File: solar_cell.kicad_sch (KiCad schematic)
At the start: 17 parts, among them U5 LM324, U6 4046

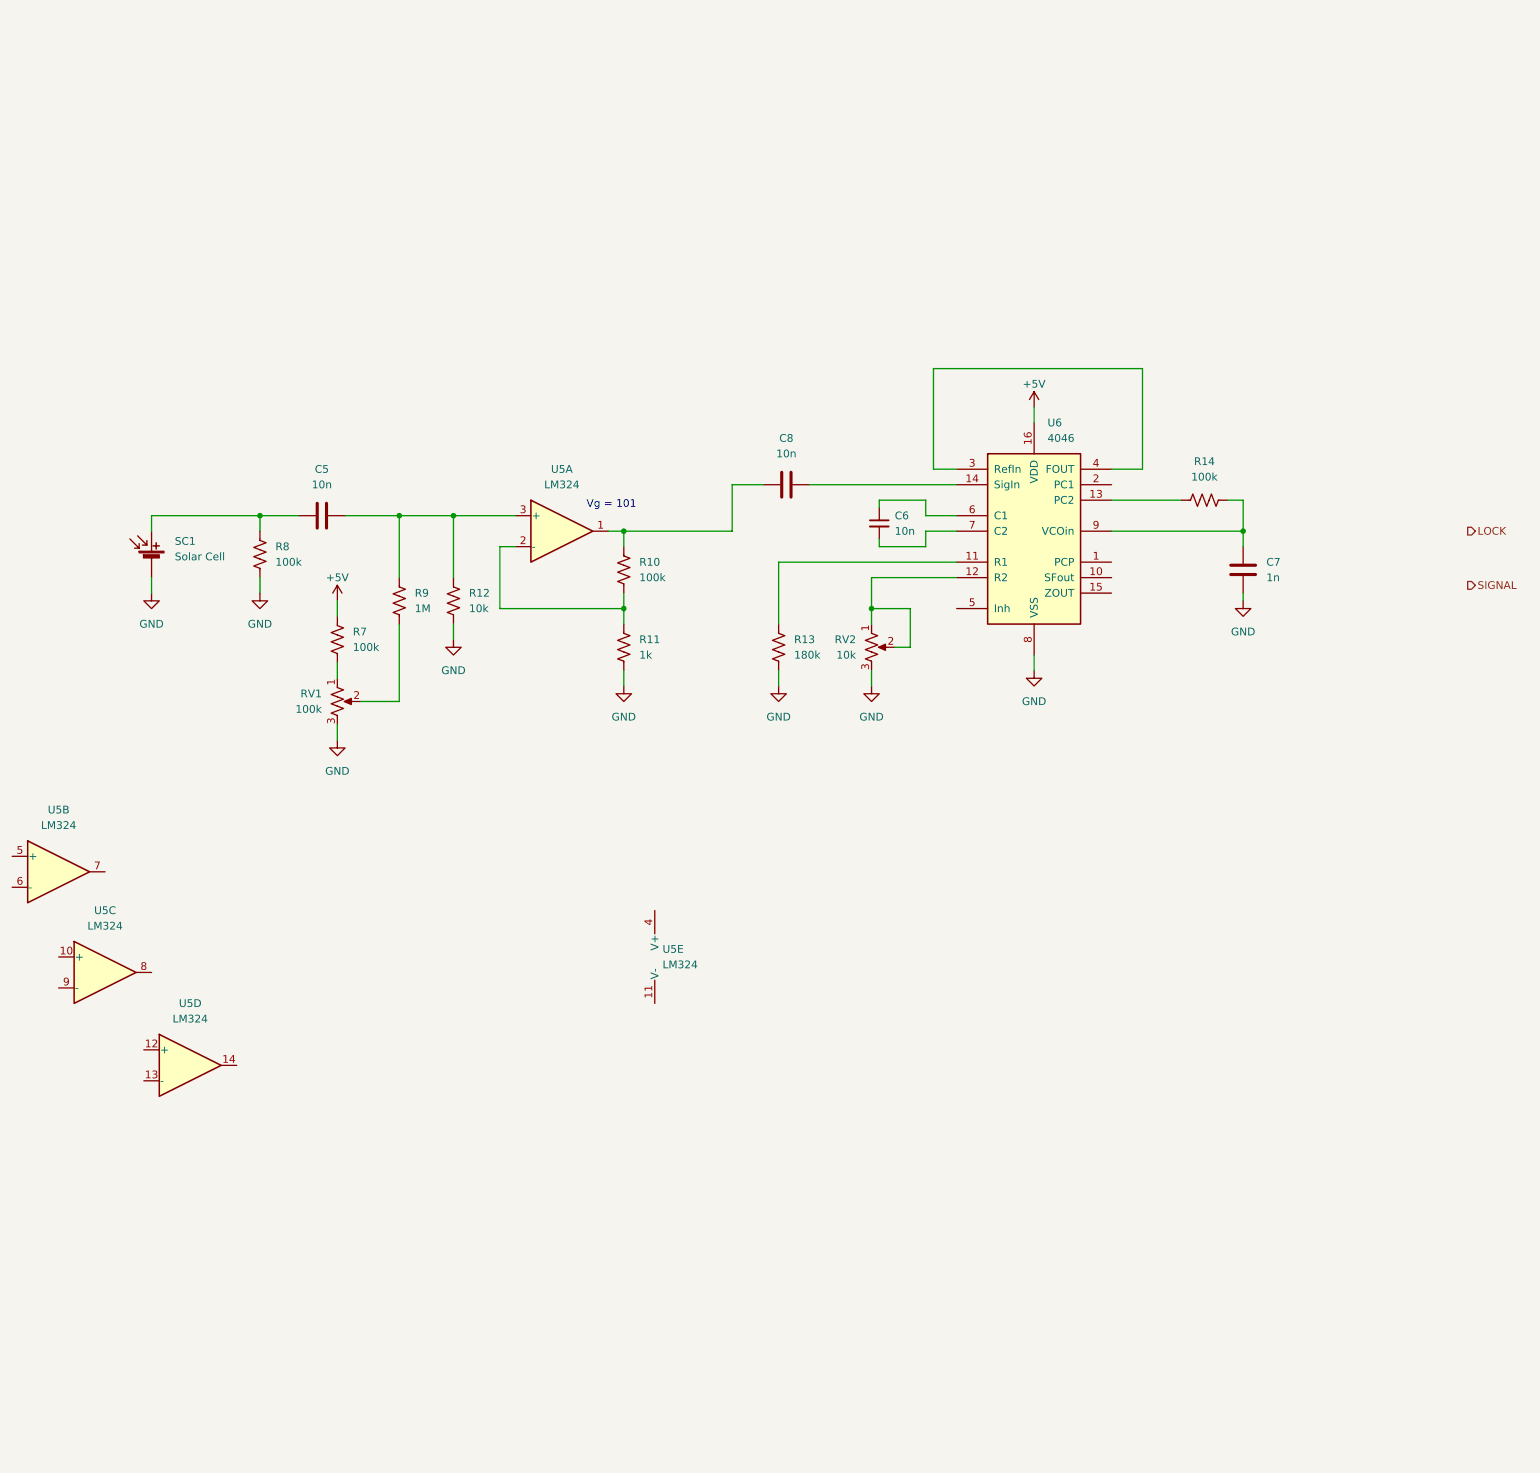
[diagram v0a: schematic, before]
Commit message: BUtton logic and solar detection
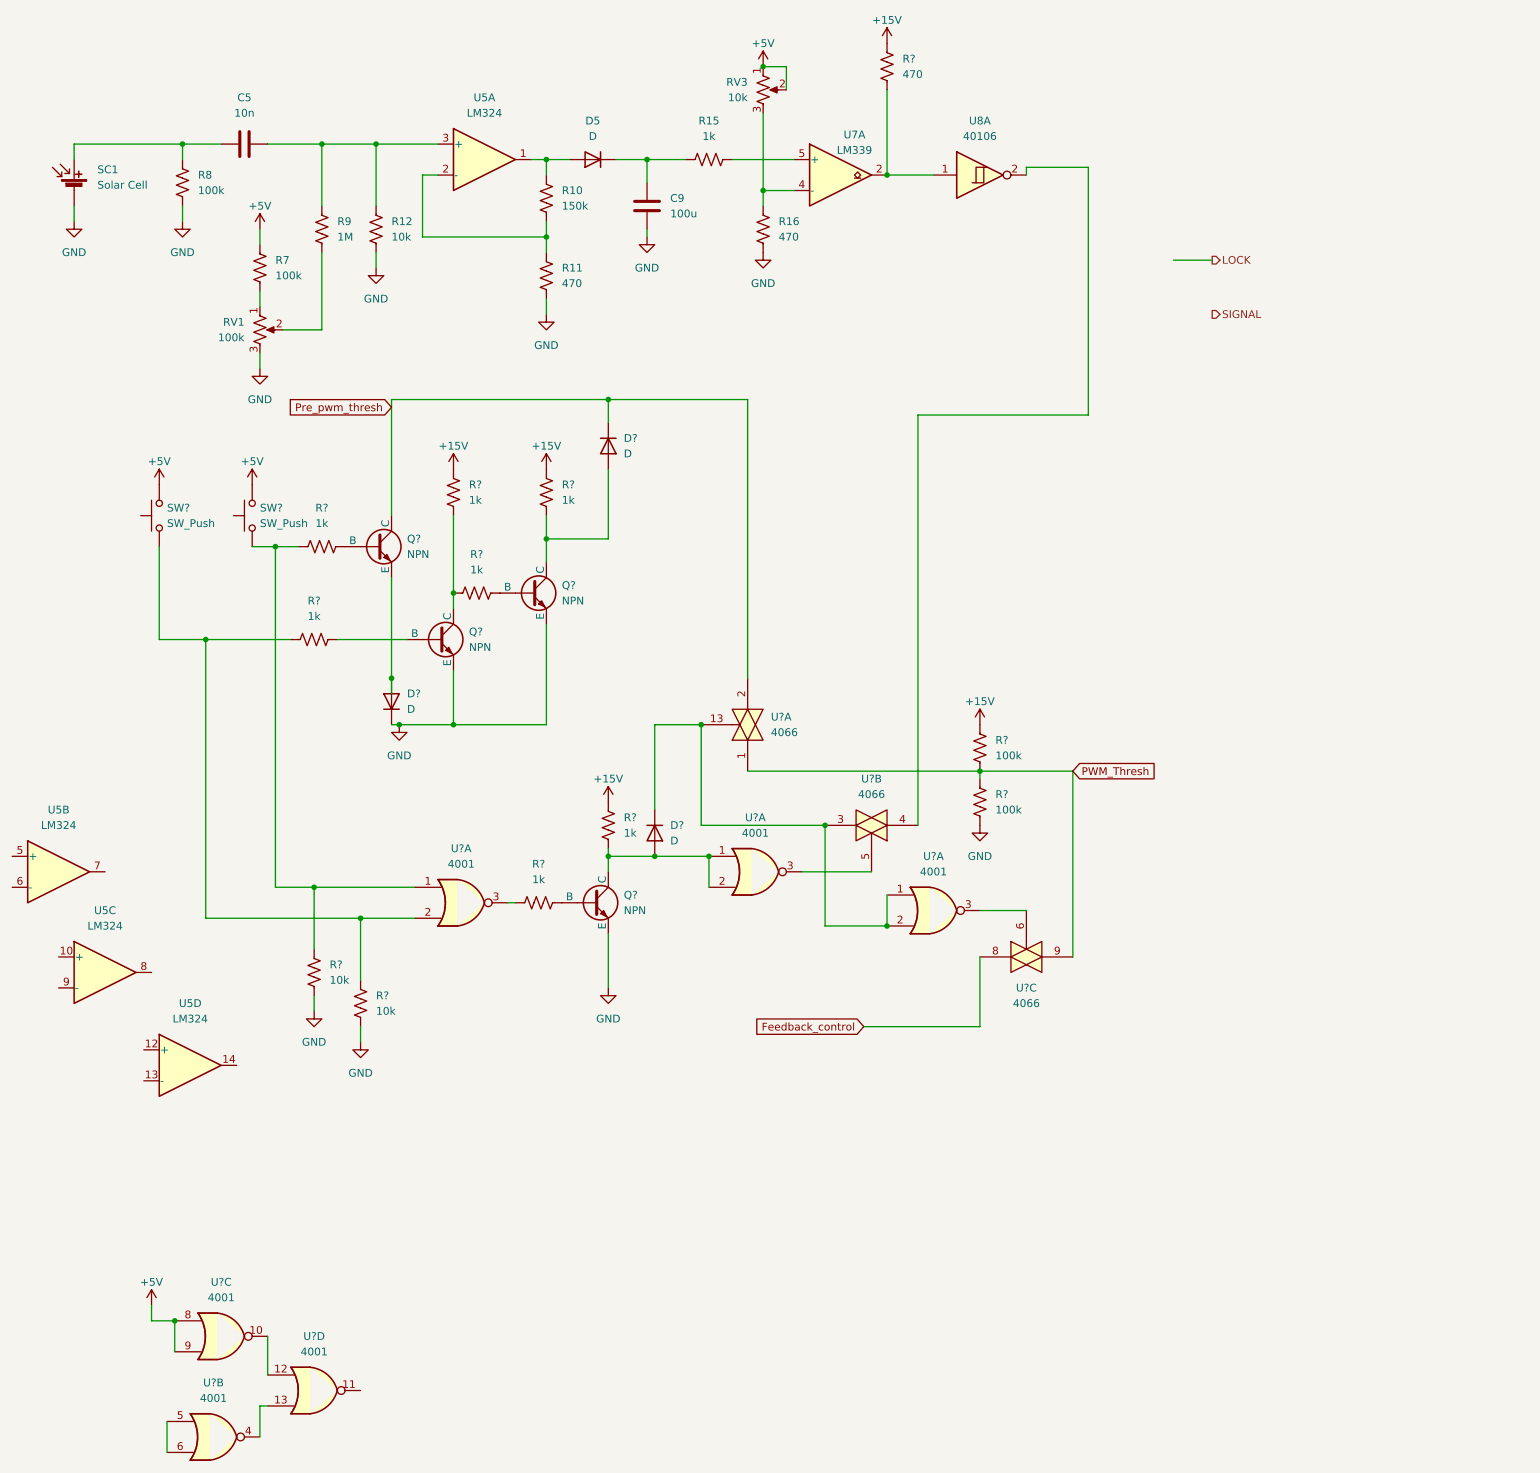
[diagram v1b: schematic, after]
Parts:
- removed C6: 10n, symbol Device:C_Small
- removed C7: 1n, symbol Device:C
- removed C8: 10n, symbol Device:C
- removed R13: 180k, symbol Device:R_US
- removed R14: 100k, symbol Device:R_US
- removed RV2: 10k, symbol Device:R_Potentiometer_US
- removed unit 5 of U5
- removed U6: 4046, symbol 4xxx:4046
- added C9: 100u, symbol Device:C
- added D5, D? (x3): D, symbol Device:D
- added Q? (x4): NPN, symbol Simulation_SPICE:NPN
- added R15, R? (x7): 1k, symbol Device:R_US
- added R16, R?: 470, symbol Device:R_US
- added R? (x2): 10k, symbol Device:R_US
- added R? (x2): 100k, symbol Device:R_US
- added RV3: 10k, symbol Device:R_Potentiometer_US
- added SW? (x2): SW_Push, symbol Switch:SW_Push
- added U7: LM339, symbol Comparator:LM339
- added U8: 40106, symbol 4xxx:40106
- added U? (x6): 4001, symbol 4xxx:4001
- added U? (x3): 4066, symbol 4xxx:4066
- R10: value 100k -> 150k
- R11: value 1k -> 470
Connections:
- net +5V: now also RV3.1, RV3.2, SW?.2, SW?.2, U?.8, U?.9
- net GND: now also C9.1, D?.1 (K), Q?.3 (E), Q?.3 (E), Q?.3 (E), R16.2, R?.1, R?.2, R?.2
- net at R10.1, U5.1: now also D5.2 (A)
- new net: C9.2, D5.1 (K), R15.1
- new net: R15.2, U7.5 (+)
- new net: U?.10, U?.12
- new net: Q?.2 (B), R?.1 (x2)
- new net: Q?.1 (C), R?.1, R?.2
- new net: D?.2 (A), Q?.1 (C), R?.1
- new net: R?.1, R?.1, SW?.1, U?.1
- new net: U?.3, U?.6
- new net: Q?.2 (B), R?.2 (x2)
- new net: D?.2 (A), Q?.1 (C), R?.1, U?.1, U?.2
- new net: D?.1 (K), U?.1, U?.13, U?.2, U?.3
- new net: U8.2, U?.4
- new net: U?.3, U?.5
- new net: R?.1, R?.1, SW?.1, U?.2
- new net: D?.2 (A), Q?.3 (E)
- new net: R16.1, RV3.3, U7.4 (-)
- new net: R?.2, U?.3
- new net: U?.13, U?.4
- new net: U?.5, U?.6
- new net: R?.2, U7.2, U8.1
- new net +15V: R?.1, R?.2, R?.2, R?.2, R?.2
- new net Feedback_control: U?.8
- new net PWM_Thresh: R?.1, R?.2, U?.1, U?.9
- new net Pre_pwm_thresh: D?.1 (K), Q?.1 (C), U?.2
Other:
- note removed: "Vg = 101"
- moved on the sheet: C5, R10, R11, R12, R7, R8, R9, RV1, SC1, U5A
